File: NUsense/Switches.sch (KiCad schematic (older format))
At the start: 6 parts

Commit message: Update NUsense Files
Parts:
- added LS?: Speaker, symbol Speaker
- added Q?: 2N3055, TO_SOT_Packages_THT:TO-3, symbol 2N3055
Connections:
- net GND: now also Q?.2 (E)
- net VDD3o3V: now also LS?.1
- new net: LS?.2, Q?.3 (C)
- new net BUZZER_SIG: Q?.1 (B)
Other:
- note added: "Buzzer"
- note added: "System Reset"
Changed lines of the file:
@@
 LIBS:NUbots
 LIBS:STM32F746ZGT6
+LIBS:Header_Connectors
 LIBS:NUsense-cache
 EELAYER 25 0
@@
 $Descr A3 16535 11693
 encoding utf-8
-Sheet 4 4
+Sheet 4 9
 Title ""
 Date ""
@@
 MCU_NRESET
 Connection ~ 4400 1800
+Text Notes 1950 3000 0    60   ~ 0
+System Reset
+Text GLabel 1350 4250 0    60   Input ~ 0
+BUZZER_SIG
+$Comp
+L GND #PWR?
+U 1 1 5A6A7F67
+P 1950 4650
+F 0 "#PWR?" H 1950 4400 50  0001 C CNN
+F 1 "GND" H 1950 4500 50  0000 C CNN
+F 2 "" H 1950 4650 50  0001 C CNN
+F 3 "" H 1950 4650 50  0001 C CNN
+	1    1950 4650
+	1    0    0    -1
+$EndComp
+$Comp
+L 2N3055 Q?
+U 1 1 5A6A7F87
+P 1850 4250
+F 0 "Q?" H 2050 4325 50  0000 L CNN
+F 1 "2N3055" H 2050 4250 50  0000 L CNN
+F 2 "TO_SOT_Packages_THT:TO-3" H 2050 4175 50  0001 L CIN
+F 3 "" H 1850 4250 50  0001 L CNN
+	1    1850 4250
+	1    0    0    -1
+$EndComp
+$Comp
+L Speaker LS?
+U 1 1 5A6A7FD9
+P 2400 3750
+F 0 "LS?" H 2450 3975 50  0000 R CNN
+F 1 "Speaker" H 2450 3900 50  0000 R CNN
+F 2 "" H 2400 3550 50  0001 C CNN
+F 3 "" H 2390 3700 50  0001 C CNN
+	1    2400 3750
+	1    0    0    -1
+$EndComp
+Wire Wire Line
+	1350 4250 1650 4250
+Wire Wire Line
+	1950 4050 1950 3850
+Wire Wire Line
+	1950 3850 2200 3850
+Wire Wire Line
+	1950 4650 1950 4450
+Text GLabel 1950 3650 1    60   Input ~ 0
+VDD3o3V
+Wire Wire Line
+	1950 3650 1950 3750
+Wire Wire Line
+	1950 3750 2200 3750
+Text Notes 1150 4750 0    60   ~ 0
+Buzzer
 $EndSCHEMATC

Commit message: Change hierarchy layout
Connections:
- net MCU_NRESET renamed MCU_RESET
- net VDD3o3V renamed +3V3
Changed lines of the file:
@@
 LIBS:valves
 LIBS:ADM6713RAKS
+LIBS:Header_Connectors
 LIBS:MPU6000
 LIBS:NUbots
 LIBS:STM32F746ZGT6
-LIBS:Header_Connectors
 LIBS:NUsense-cache
 EELAYER 25 0
@@
 	1    0    0    -1
 $EndComp
-Text GLabel 2650 1400 1    60   Input ~ 0
-VDD3o3V
 Wire Wire Line
 	2650 1400 2650 1650
@@
 Wire Wire Line
 	4400 2000 4400 2150
-Text GLabel 4700 1800 2    60   Input ~ 0
-MCU_NRESET
 Connection ~ 4400 1800
 Text Notes 1950 3000 0    60   ~ 0
 System Reset
-Text GLabel 1350 4250 0    60   Input ~ 0
-BUZZER_SIG
 $Comp
 L GND #PWR?
@@
 Wire Wire Line
 	1950 4650 1950 4450
-Text GLabel 1950 3650 1    60   Input ~ 0
-VDD3o3V
 Wire Wire Line
 	1950 3650 1950 3750
@@
 Text Notes 1150 4750 0    60   ~ 0
 Buzzer
+$Comp
+L +3.3V #PWR?
+U 1 1 5A6FD90A
+P 2650 1400
+F 0 "#PWR?" H 2650 1250 50  0001 C CNN
+F 1 "+3.3V" H 2650 1540 50  0000 C CNN
+F 2 "" H 2650 1400 50  0001 C CNN
+F 3 "" H 2650 1400 50  0001 C CNN
+	1    2650 1400
+	1    0    0    -1
+$EndComp
+$Comp
+L +3.3V #PWR?
+U 1 1 5A6FD934
+P 1950 3650
+F 0 "#PWR?" H 1950 3500 50  0001 C CNN
+F 1 "+3.3V" H 1950 3790 50  0000 C CNN
+F 2 "" H 1950 3650 50  0001 C CNN
+F 3 "" H 1950 3650 50  0001 C CNN
+	1    1950 3650
+	1    0    0    -1
+$EndComp
+Text HLabel 1350 4250 0    60   Input ~ 0
+BUZZER_SIG
+Text HLabel 4700 1800 2    60   Output ~ 0
+MCU_RESET
 $EndSCHEMATC

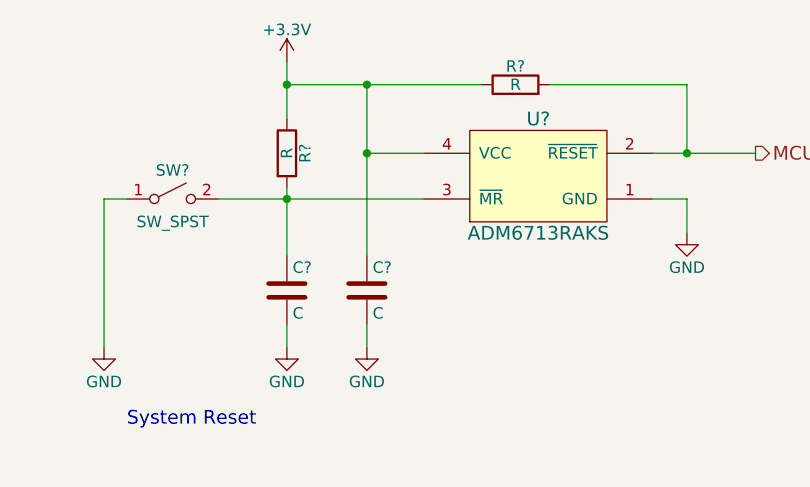
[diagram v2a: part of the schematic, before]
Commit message: Update component values
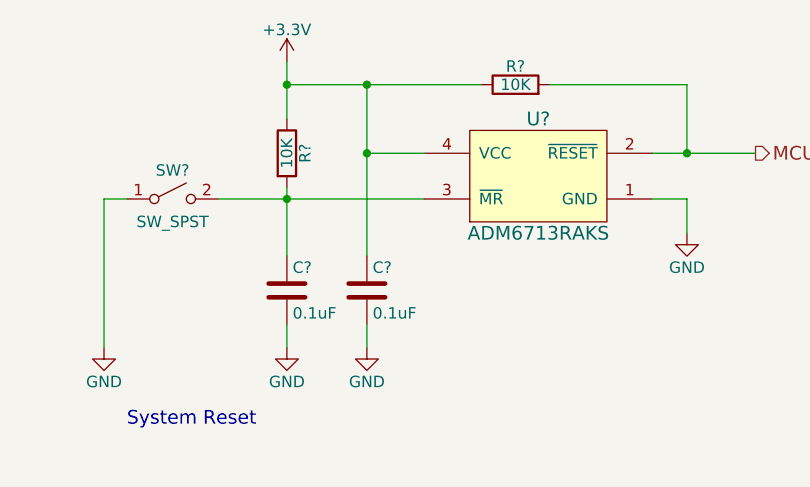
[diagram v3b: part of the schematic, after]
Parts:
- removed C?: C, symbol C
- removed R?: R, symbol R
- added C?: 0.1uF, symbol C
- added R?: 10K, symbol R
- C?: value C -> 0.1uF
- R?: value R -> 10K
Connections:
- net +3V3: now also C?.1, R?.1
- net GND: now also C?.2
- net MCU_RESET: now also R?.2
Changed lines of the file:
@@
-$Comp
-L C C?
-U 1 1 5A6C0F0D
-P 3000 2400
-F 0 "C?" H 3025 2500 50  0000 L CNN
-F 1 "C" H 3025 2300 50  0000 L CNN
-F 2 "" H 3038 2250 50  0001 C CNN
-F 3 "" H 3000 2400 50  0001 C CNN
-	1    3000 2400
-	1    0    0    -1
-$EndComp
 $Comp
 L C C?
@@
 P 2650 2400
 F 0 "C?" H 2675 2500 50  0000 L CNN
-F 1 "C" H 2675 2300 50  0000 L CNN
+F 1 "0.1uF" H 2675 2300 50  0000 L CNN
 F 2 "" H 2688 2250 50  0001 C CNN
 F 3 "" H 2650 2400 50  0001 C CNN
@@
 P 2650 1800
 F 0 "R?" V 2730 1800 50  0000 C CNN
-F 1 "R" V 2650 1800 50  0000 C CNN
+F 1 "10K" V 2650 1800 50  0000 C CNN
 F 2 "" V 2580 1800 50  0001 C CNN
 F 3 "" H 2650 1800 50  0001 C CNN
@@
 	1    4400 2150
 	1    0    0    -1
-$EndComp
-$Comp
-L R R?
-U 1 1 5A6C0F4F
-P 3650 1500
-F 0 "R?" V 3730 1500 50  0000 C CNN
-F 1 "R" V 3650 1500 50  0000 C CNN
-F 2 "" V 3580 1500 50  0001 C CNN
-F 3 "" H 3650 1500 50  0001 C CNN
-	1    3650 1500
-	0    -1   -1   0
 $EndComp
 Connection ~ 3000 1500
@@
 Text HLabel 4700 1800 2    60   Output ~ 0
 MCU_RESET
+$Comp
+L C C?
+U 1 1 5A704C77
+P 3000 2400
+F 0 "C?" H 3025 2500 50  0000 L CNN
+F 1 "0.1uF" H 3025 2300 50  0000 L CNN
+F 2 "" H 3038 2250 50  0001 C CNN
+F 3 "" H 3000 2400 50  0001 C CNN
+	1    3000 2400
+	1    0    0    -1
+$EndComp
+$Comp
+L R R?
+U 1 1 5A704CB3
+P 3650 1500
+F 0 "R?" V 3730 1500 50  0000 C CNN
+F 1 "10K" V 3650 1500 50  0000 C CNN
+F 2 "" V 3580 1500 50  0001 C CNN
+F 3 "" H 3650 1500 50  0001 C CNN
+	1    3650 1500
+	0    -1   -1   0
+$EndComp
 $EndSCHEMATC
